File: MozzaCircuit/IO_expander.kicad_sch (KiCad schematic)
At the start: 2 parts, among them J1 RJ45, U1 MCP23017_ML

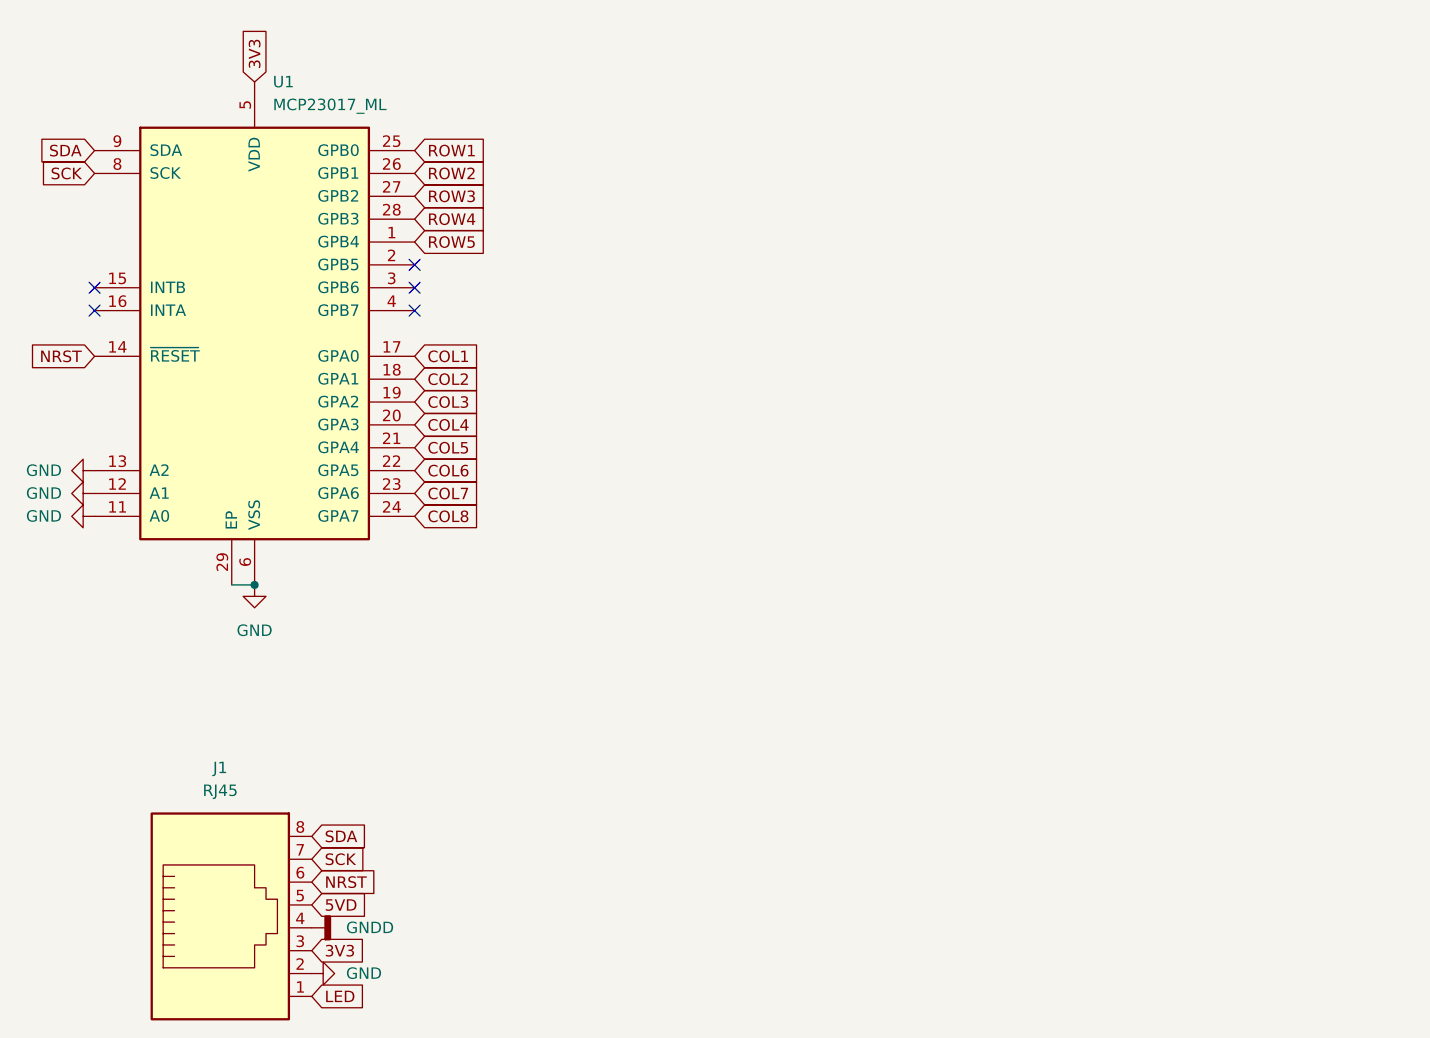
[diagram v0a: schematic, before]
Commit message: added rotary encoder
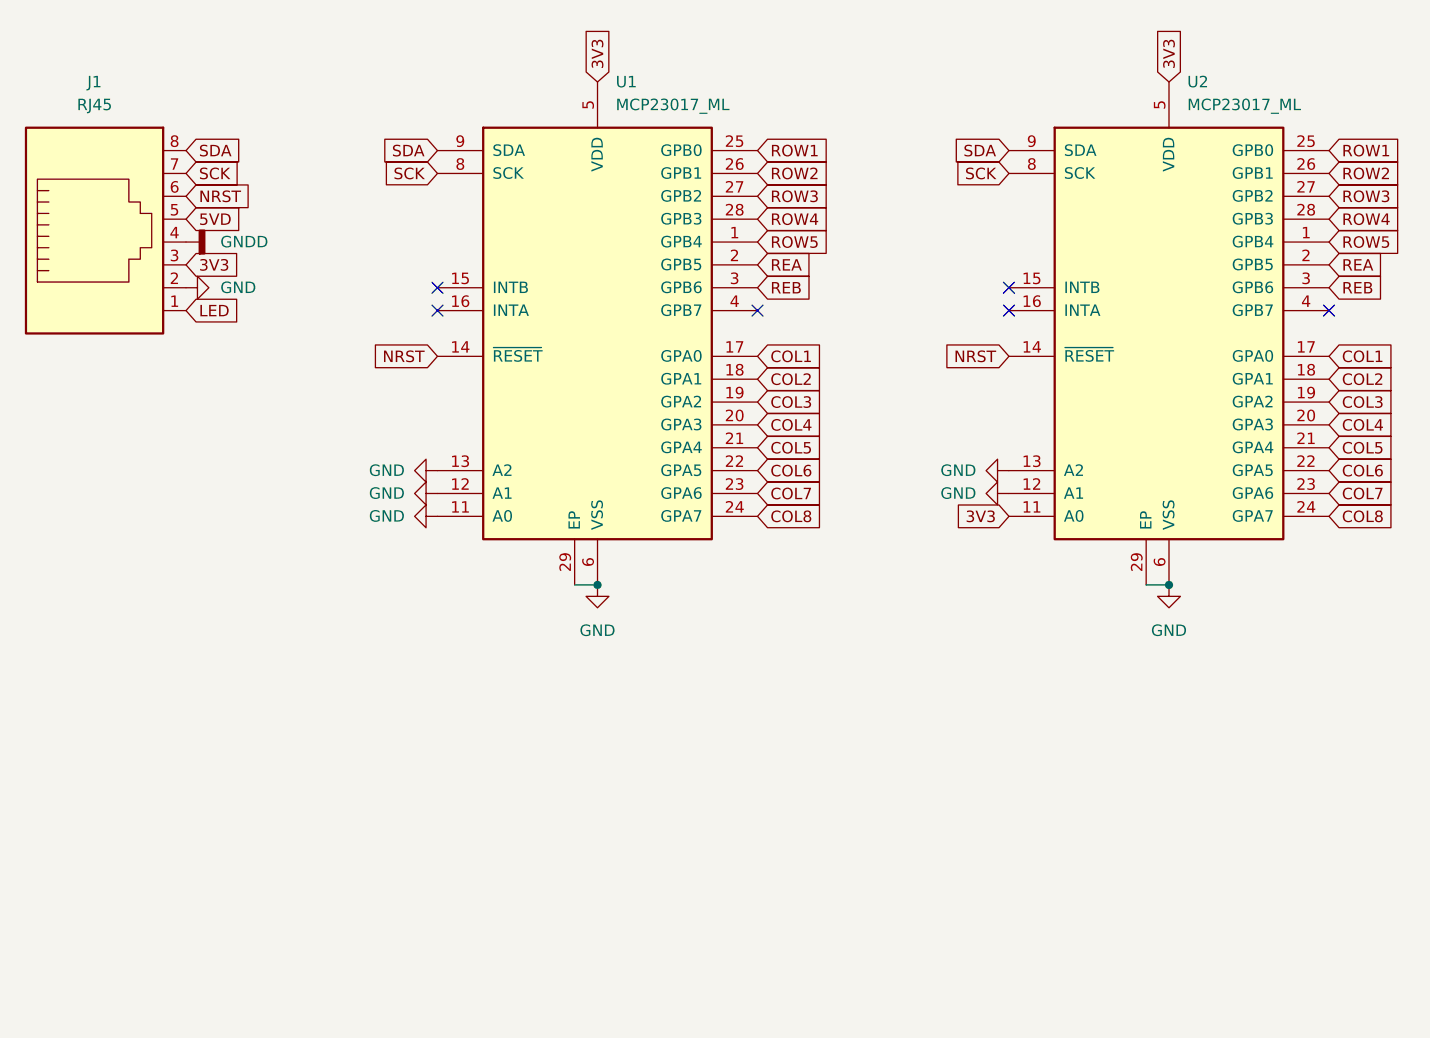
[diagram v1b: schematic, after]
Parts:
- added U2: MCP23017_ML, Package_DFN_QFN:QFN-28-1EP_6x6mm_P0.65mm_EP4.25x4.25mm, symbol Interface_Expansion:MCP23017_ML
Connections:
- net 3V3: now also U2.11 (A0), U2.5 (VDD)
- net COL1: now also U2.17 (GPA0)
- net COL2: now also U2.18 (GPA1)
- net COL3: now also U2.19 (GPA2)
- net COL4: now also U2.20 (GPA3)
- net COL5: now also U2.21 (GPA4)
- net COL6: now also U2.22 (GPA5)
- net COL7: now also U2.23 (GPA6)
- net COL8: now also U2.24 (GPA7)
- net GND: now also U2.12 (A1), U2.13 (A2), U2.29 (EP), U2.6 (VSS)
- net NRST: now also U2.14 (~{RESET})
- net ROW1: now also U2.25 (GPB0)
- net ROW2: now also U2.26 (GPB1)
- net ROW3: now also U2.27 (GPB2)
- net ROW4: now also U2.28 (GPB3)
- net ROW5: now also U2.1 (GPB4)
- net SCK: now also U2.8 (SCK)
- net SDA: now also U2.9 (SDA)
- net REA: now reaches U1.2 (GPB5)
- net REA: now also U2.2 (GPB5)
- net REB: now reaches U1.3 (GPB6)
- net REB: now also U2.3 (GPB6)
- no-connect marks 5 -> 6
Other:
- moved on the sheet: J1, U1

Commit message: led matrix
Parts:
- removed J1: RJ45, symbol Connector:RJ45
- removed U1, U2: MCP23017_ML, Package_DFN_QFN:QFN-28-1EP_6x6mm_P0.65mm_EP4.25x4.25mm, symbol Interface_Expansion:MCP23017_ML
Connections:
- no-connect marks 6 -> 0
